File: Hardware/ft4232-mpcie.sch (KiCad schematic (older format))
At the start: 1 part, among them U1 MPCIE-Socket

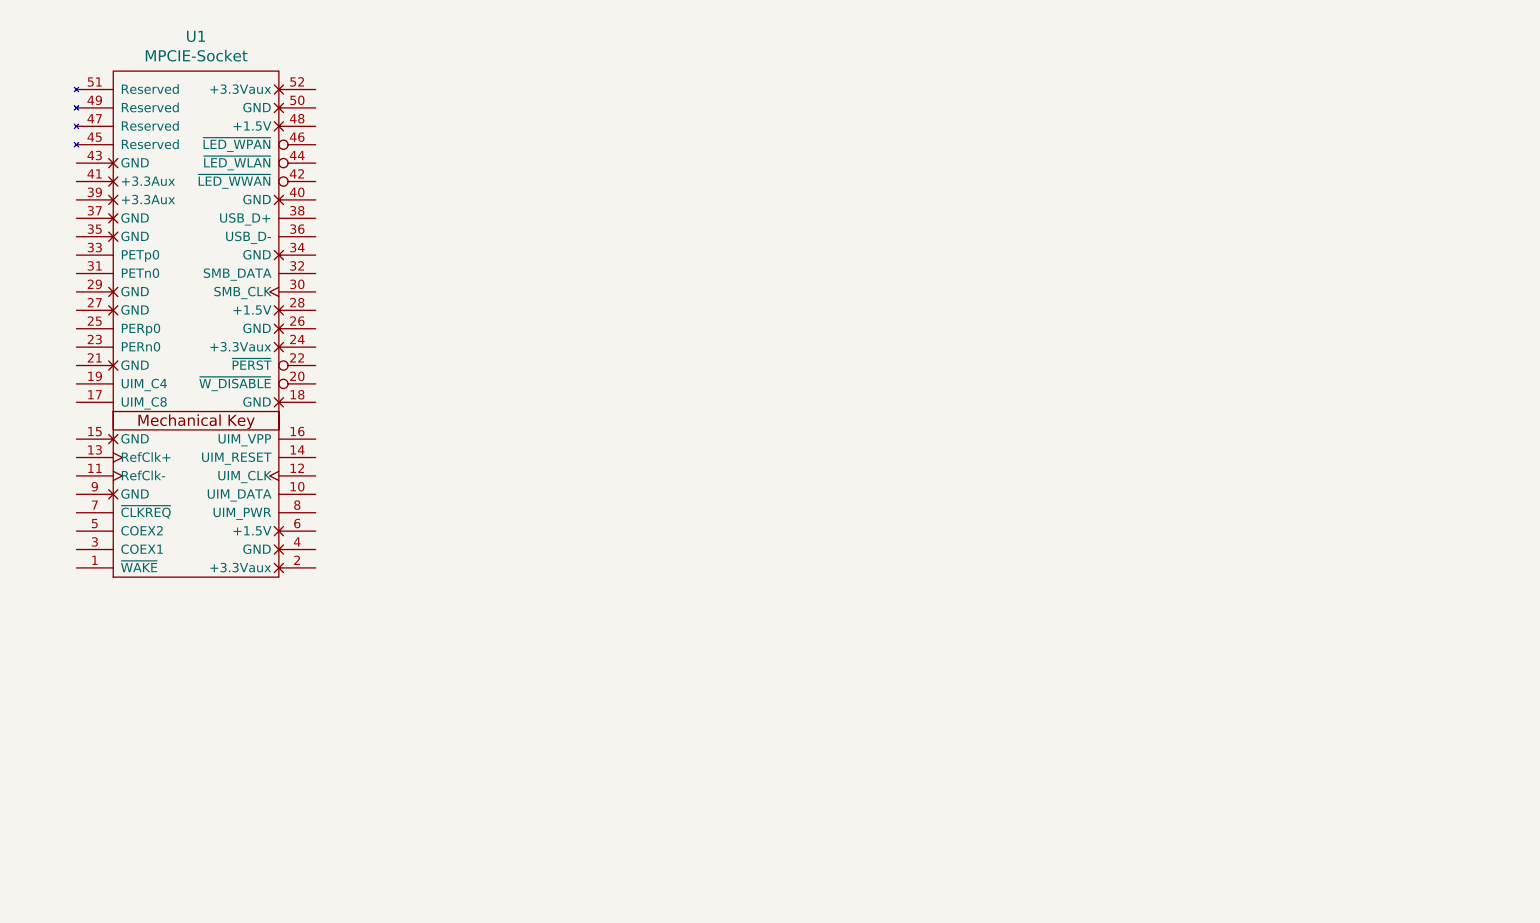
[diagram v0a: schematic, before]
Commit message: update pcb component
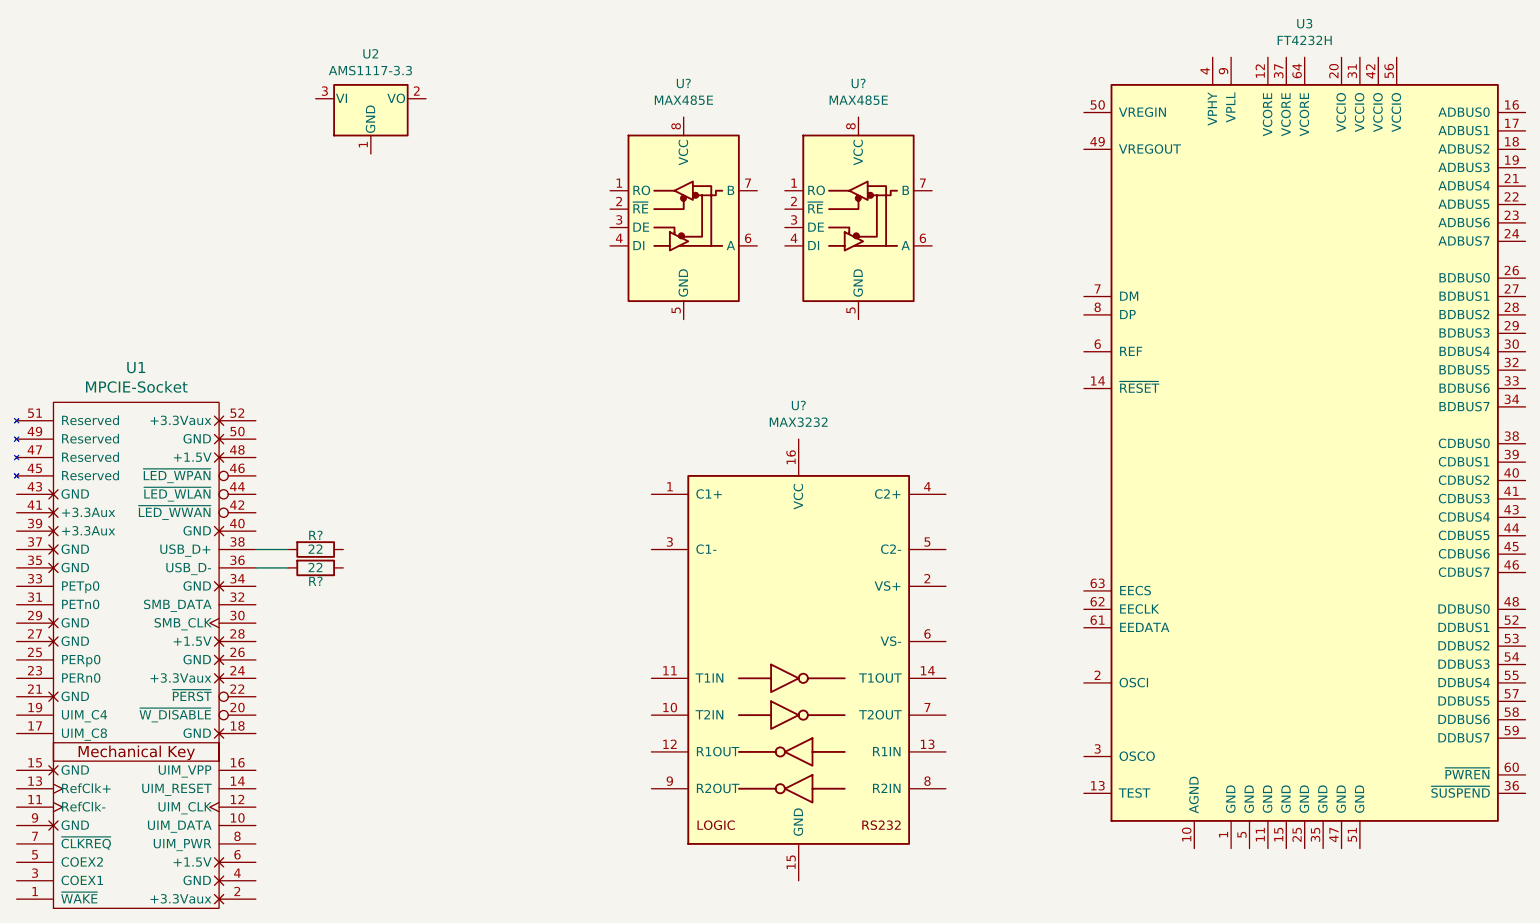
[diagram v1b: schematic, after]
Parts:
- added R? (x2): 22, symbol Device:R
- added U2: AMS1117-3.3, Package_TO_SOT_SMD:SOT-223-3_TabPin2, symbol Regulator_Linear:AMS1117-3.3
- added U3: FT4232H, Package_DFN_QFN:QFN-64-1EP_9x9mm_P0.5mm_EP6x6mm, symbol Interface_USB:FT4232H
- added U?: MAX3232, symbol Interface_UART:MAX3232
- added U? (x2): MAX485E, symbol Interface_UART:MAX485E
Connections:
- net at U1.36 (USB_D-): now also R?.2
- net at U1.38 (USB_D+): now also R?.2
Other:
- moved on the sheet: U1
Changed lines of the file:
@@
 EESchema Schematic File Version 4
-LIBS:mpcie-3serial-cache
+LIBS:ft4232-mpcie-cache
 EELAYER 30 0
 EELAYER END
@@
 L mpcie:MPCIE-Socket U1
 U 1 1 5D6BE575
-P 2600 2800
-F 0 "U1" H 2600 4237 60  0000 C CNN
-F 1 "MPCIE-Socket" H 2600 4131 60  0000 C CNN
-F 2 "mpcie:mpcie-full-card" H 2700 1800 60  0001 C CNN
-F 3 "" H 2700 1800 60  0000 C CNN
-	1    2600 2800
+P 2275 4600
+F 0 "U1" H 2275 6037 60  0000 C CNN
+F 1 "MPCIE-Socket" H 2275 5931 60  0000 C CNN
+F 2 "mpcie:mpcie-full-card" H 2375 3600 60  0001 C CNN
+F 3 "" H 2375 3600 60  0000 C CNN
+	1    2275 4600
 	1    0    0    -1
 $EndComp
+$Comp
+L Interface_USB:FT4232H U3
+U 1 1 5D74C98D
+P 8625 3675
+F 0 "U3" H 8625 6056 50  0000 C CNN
+F 1 "FT4232H" H 8625 5965 50  0000 C CNN
+F 2 "Package_DFN_QFN:QFN-64-1EP_9x9mm_P0.5mm_EP6x6mm" H 8625 3675 50  0001 C CNN
+F 3 "" H 8625 3675 50  0001 C CNN
+	1    8625 3675
+	1    0    0    -1
+$EndComp
+$Comp
+L Regulator_Linear:AMS1117-3.3 U2
+U 1 1 5D75436C
+P 3550 1700
+F 0 "U2" H 3550 1942 50  0000 C CNN
+F 1 "AMS1117-3.3" H 3550 1851 50  0000 C CNN
+F 2 "Package_TO_SOT_SMD:SOT-223-3_TabPin2" H 3550 1900 50  0001 C CNN
+F 3 "http://www.advanced-monolithic.com/pdf/ds1117.pdf" H 3650 1450 50  0001 C CNN
+	1    3550 1700
+	1    0    0    -1
+$EndComp
+$Comp
+L Device:R R?
+U 1 1 5D756FD7
+P 3250 4150
+F 0 "R?" V 3175 4150 50  0000 C CNN
+F 1 "22" V 3250 4150 50  0000 C CNN
+F 2 "" V 3180 4150 50  0001 C CNN
+F 3 "~" H 3250 4150 50  0001 C CNN
+	1    3250 4150
+	0    1    1    0
+$EndComp
+$Comp
+L Device:R R?
+U 1 1 5D7581C5
+P 3250 4250
+F 0 "R?" V 3325 4250 50  0000 C CNN
+F 1 "22" V 3250 4250 50  0000 C CNN
+F 2 "" V 3180 4250 50  0001 C CNN
+F 3 "~" H 3250 4250 50  0001 C CNN
+	1    3250 4250
+	0    1    1    0
+$EndComp
+Wire Wire Line
+	2925 4150 3100 4150
+Wire Wire Line
+	2925 4250 3100 4250
+$Comp
+L Interface_UART:MAX3232 U?
+U 1 1 5D759314
+P 5875 4750
+F 0 "U?" H 5875 6131 50  0000 C CNN
+F 1 "MAX3232" H 5875 6040 50  0000 C CNN
+F 2 "" H 5925 3700 50  0001 L CNN
+F 3 "https://datasheets.maximintegrated.com/en/ds/MAX3222-MAX3241.pdf" H 5875 4850 50  0001 C CNN
+	1    5875 4750
+	1    0    0    -1
+$EndComp
+$Comp
+L Interface_UART:MAX485E U?
+U 1 1 5D75A1CD
+P 6200 2300
+F 0 "U?" H 6200 2981 50  0000 C CNN
+F 1 "MAX485E" H 6200 2890 50  0000 C CNN
+F 2 "" H 6200 1600 50  0001 C CNN
+F 3 "https://datasheets.maximintegrated.com/en/ds/MAX1487E-MAX491E.pdf" H 6200 2350 50  0001 C CNN
+	1    6200 2300
+	1    0    0    -1
+$EndComp
+$Comp
+L Interface_UART:MAX485E U?
+U 1 1 5D75AD32
+P 5250 2300
+F 0 "U?" H 5250 2981 50  0000 C CNN
+F 1 "MAX485E" H 5250 2890 50  0000 C CNN
+F 2 "" H 5250 1600 50  0001 C CNN
+F 3 "https://datasheets.maximintegrated.com/en/ds/MAX1487E-MAX491E.pdf" H 5250 2350 50  0001 C CNN
+	1    5250 2300
+	1    0    0    -1
+$EndComp
